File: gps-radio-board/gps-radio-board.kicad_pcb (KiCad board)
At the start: 4 copper layers, 25 x 54 mm, 62 parts, among them J1 SMA, J2 SMA, J3 USB_C_Receptacle_USB2.0_16P, J4 JST_BATT, J5 Conn_01x04, J6 Conn_01x04, J7 Conn_01x04, J8 DM3CS-SF, U1 ESP32-C6-MINI-1U-H4, U3 SiP32431DR3, U4 AP2112K-3.3, U5 MAX-M10N, U6 MCP73831, U7 AP2112K-3.3

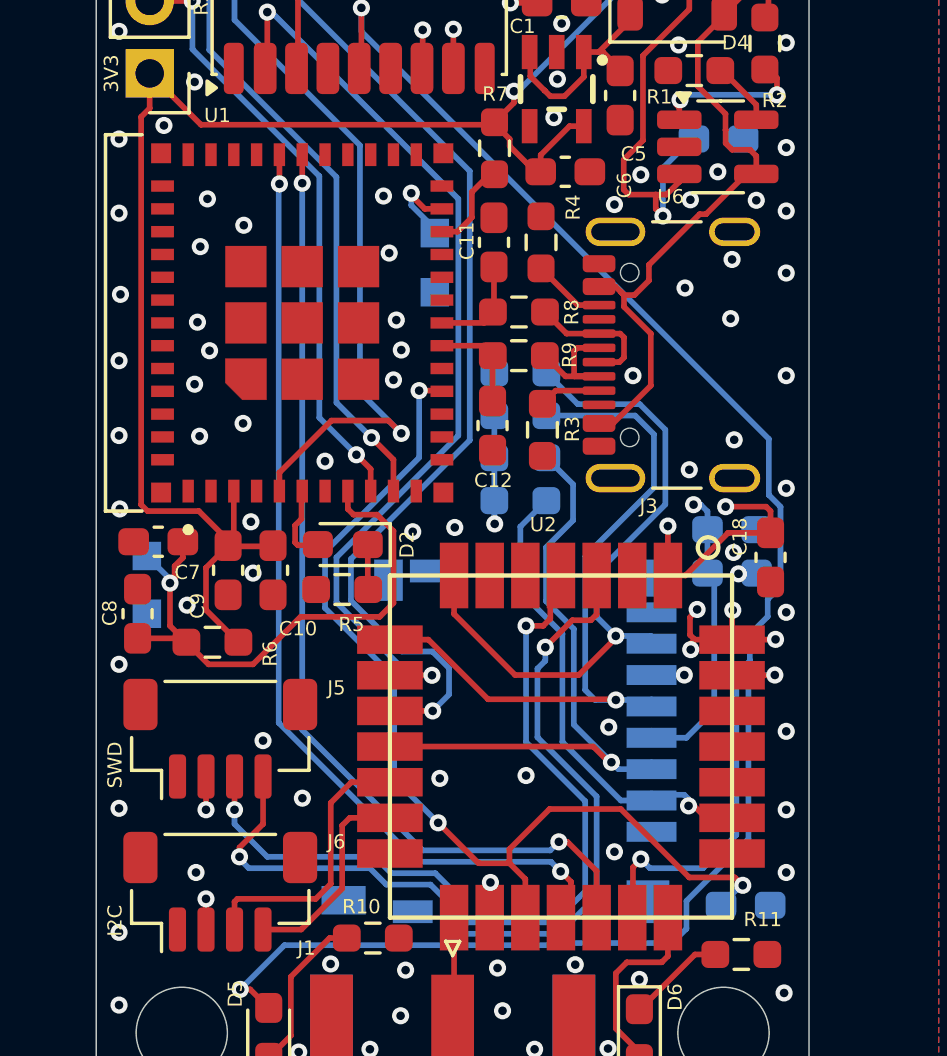
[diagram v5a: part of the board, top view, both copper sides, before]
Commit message: Add input cap for battery
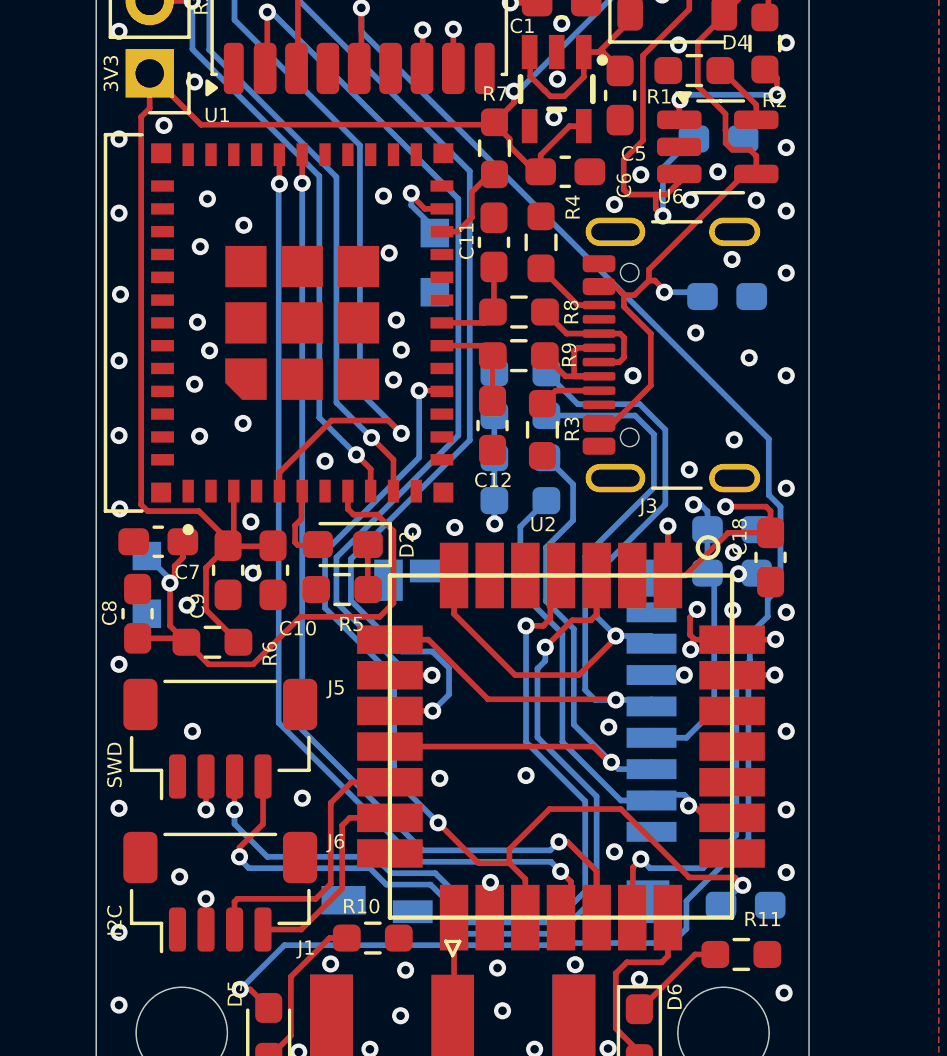
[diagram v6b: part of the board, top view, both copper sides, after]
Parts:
- added C21: 4.7u, Capacitor_SMD:C_0603_1608Metric_Pad1.08x0.95mm_HandSolder, B.Cu at (109.6, 98.2)
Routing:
- net /USB_IN: track 25.5 -> 27.5 mm, vias 0 -> 1
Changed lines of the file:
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@@
 	(footprint "Capacitor_SMD:C_0603_1608Metric_Pad1.08x0.95mm_HandSolder"
 		(layer "B.Cu")
+		(at 109.625 98.175)
+		(descr "Capacitor SMD 0603 (1608 Metric), square (rectangular) end terminal, IPC-7351 nominal with elongated pad for handsoldering. (Body size source: IPC-SM-782 page 76, https://www.pcb-3d.com/wordpress/wp-content/uploads/ipc-sm-782a_amendment_1_and_2.pdf)")
+		(tags "capacitor handsolder")
+		(property "Reference" "C21"
+			(at 0 1.43 0)
+			(layer "B.SilkS")
+			(effects
+				(font
+					(size 0.5 0.5)
+					(thickness 0.07)
+				)
+				(justify mirror)
+			)
+		)
+		(property "Value" "4.7u"
+			(at 0 -1.43 0)
+			(layer "B.Fab")
+			(effects
+				(font
+					(size 1 1)
+					(thickness 0.15)
+				)
+				(justify mirror)
+			)
+		)
+		(property "Datasheet" ""
+			(at 0 0 0)
+			(layer "B.Fab")
+			(hide yes)
+			(effects
+				(font
+					(size 1.27 1.27)
+				)
+				(justify mirror)
+			)
+		)
+		(property "Description" "Unpolarized capacitor"
+			(at 0 0 0)
+			(layer "B.Fab")
+			(hide yes)
+			(effects
+				(font
+					(size 1.27 1.27)
+				)
+				(justify mirror)
+			)
+		)
+		(property ki_fp_filters "C_*")
+		(sheetname "/")
+		(sheetfile "gps-radio-board.kicad_sch")
+		(units
+			(unit
+				(name "A")
+				(pins "1" "2")
+			)
+		)
+		(attr smd)
+		(duplicate_pad_numbers_are_jumpers no)
+		(fp_line
+			(start -0.146267 -0.51)
+			(end 0.146267 -0.51)
+			(stroke
+				(width 0.12)
+				(type solid)
+			)
+			(layer "B.SilkS")
+		)
+		(fp_line
+			(start -0.146267 0.51)
+			(end 0.146267 0.51)
+			(stroke
+				(width 0.12)
+				(type solid)
+			)
+			(layer "B.SilkS")
+		)
+		(fp_rect
+			(start -1.65 0.73)
+			(end 1.65 -0.73)
+			(stroke
+				(width 0.05)
+				(type solid)
+			)
+			(fill no)
+			(layer "B.CrtYd")
+		)
+		(fp_rect
+			(start -0.8 0.4)
+			(end 0.8 -0.4)
+			(stroke
+				(width 0.1)
+				(type solid)
+			)
+			(fill no)
+			(layer "B.Fab")
+		)
+		(fp_text user "${REFERENCE}"
+			(at 0 0 0)
+			(layer "B.Fab")
+			(effects
+				(font
+					(size 0.4 0.4)
+					(thickness 0.06)
+				)
+				(justify mirror)
+			)
+		)
+		(pad "1" smd roundrect
+			(at -0.8625 0)
+			(size 1.075 0.95)
+			(layers "B.Cu" "B.Mask" "B.Paste")
+			(roundrect_rratio 0.25)
+			(net "/USB_IN")
+			(pintype "passive")
+		)
+		(pad "2" smd roundrect
+			(at 0.8625 0)
+			(size 1.075 0.95)
+			(layers "B.Cu" "B.Mask" "B.Paste")
+			(roundrect_rratio 0.25)
+			(net "GND")
+			(pintype "passive")
+		)
+		(embedded_fonts no)
+		(model "${KICAD10_3DMODEL_DIR}/Capacitor_SMD.3dshapes/C_0603_1608Metric.step"
+			(offset
+				(xyz 0 0 0)
+			)
+			(scale
+				(xyz 1 1 1)
+			)
+			(rotate
+				(xyz 0 0 0)
+			)
+		)
+	)
+	(footprint "Capacitor_SMD:C_0603_1608Metric_Pad1.08x0.95mm_HandSolder"
+		(layer "B.Cu")
 		(at 109.325 92.65)
 		(descr "Capacitor SMD 0603 (1608 Metric), square (rectangular) end terminal, IPC-7351 nominal with elongated pad for handsoldering. (Body size source: IPC-SM-782 page 76, https://www.pcb-3d.com/wordpress/wp-content/uploads/ipc-sm-782a_amendment_1_and_2.pdf)")
@@
 	)
 	(segment
-		(start 106.01 98.125001)
-		(end 106.374593 98.125001)
-		(width 0.2)
-		(layer "F.Cu")
-		(net "/USB_IN")
-	)
-	(segment
 		(start 109.525 88.25)
 		(end 109.525 88.325)
@@
 	)
 	(segment
-		(start 106.885 97.614594)
-		(end 106.885 97.065)
-		(width 0.2)
-		(layer "F.Cu")
-		(net "/USB_IN")
-	)
-	(segment
-		(start 106.885 97.065)
-		(end 108.6625 95.2875)
+		(start 106.885 97.2275)
+		(end 110.2375 93.875)
 		(width 0.2)
 		(layer "F.Cu")
@@
 	)
 	(segment
+		(start 106.885 97.614594)
+		(end 106.885 97.2275)
+		(width 0.2)
+		(layer "F.Cu")
+		(net "/USB_IN")
+	)
+	(segment
+		(start 106.885 97.614594)
+		(end 107.089594 97.614594)
+		(width 0.2)
+		(layer "F.Cu")
+		(net "/USB_IN")
+	)
+	(segment
 		(start 110.15 87.625)
 		(end 109.525 88.25)
@@
 	)
 	(segment
+		(start 106.01 98.125001)
+		(end 106.374593 98.125001)
+		(width 0.2)
+		(layer "F.Cu")
+		(net "/USB_IN")
+	)
+	(segment
 		(start 110.65 93.25)
 		(end 110.65 93.875)
@@
 	)
 	(segment
-		(start 109.575 92.338576)
-		(end 109.575 92.8)
+		(start 106.374593 98.125001)
+		(end 106.885 97.614594)
 		(width 0.2)
 		(layer "F.Cu")
@@
 	)
 	(segment
-		(start 110.3 93.875)
-		(end 111.225 93.875)
+		(start 107.089594 97.614594)
+		(end 107.425 97.95)
 		(width 0.2)
 		(layer "F.Cu")
@@
 	)
 	(segment
-		(start 108.8875 95.2875)
-		(end 110.3 93.875)
+		(start 109.575 92.338576)
+		(end 109.575 92.8)
 		(width 0.2)
 		(layer "F.Cu")
@@
 	)
 	(segment
-		(start 108.6625 95.2875)
-		(end 108.8875 95.2875)
+		(start 110.2375 93.875)
+		(end 111.225 93.875)
 		(width 0.2)
 		(layer "F.Cu")
@@
 	)
 	(segment
-		(start 106.374593 98.125001)
-		(end 106.885 97.614594)
-		(width 0.2)
-		(layer "F.Cu")
-		(net "/USB_IN")
-	)
-	(segment
 		(start 105.709999 97.825)
 		(end 106.01 98.125001)
@@
 		(net "/USB_IN")
 	)
+	(via
+		(at 107.425 98.025)
+		(size 0.6)
+		(drill 0.3)
+		(layers "F.Cu" "B.Cu")
+		(net "/USB_IN")
+	)
+	(segment
+		(start 107.425 98.025)
+		(end 108.6125 98.025)
+		(width 0.2)
+		(layer "B.Cu")
+		(net "/USB_IN")
+	)
+	(segment
+		(start 108.6125 98.025)
+		(end 108.7625 98.175)
+		(width 0.2)
+		(layer "B.Cu")
+		(net "/USB_IN")
+	)
 	(segment
 		(start 97.0375 108.45)
@@
 	)
 	(via
-		(at 109.75 98.95)
+		(at 110.4 100.325)
 		(size 0.6)
 		(drill 0.3)
@@
 	)
 	(via
-		(at 108.15 97.875)
+		(at 108.525 99.45)
 		(size 0.6)
 		(drill 0.3)
@@
 	)
 	(via
-		(at 91 118.375)
+		(at 90.425 118.525)
 		(size 0.6)
 		(drill 0.3)
@@
 	)
 	(via
-		(at 93.35 113.75)
+		(at 90.875 113.425)
 		(size 0.6)
 		(drill 0.3)
